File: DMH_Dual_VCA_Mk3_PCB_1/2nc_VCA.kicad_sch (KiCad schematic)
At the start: 38 parts, among them Q5 BC548, Q6 BC548, Q7 BC548, Q8 BC548, SW1 SW_DPDT_OnOffOn, SW2 SW_DPDT_3way, U3 TL074, U4 TL074

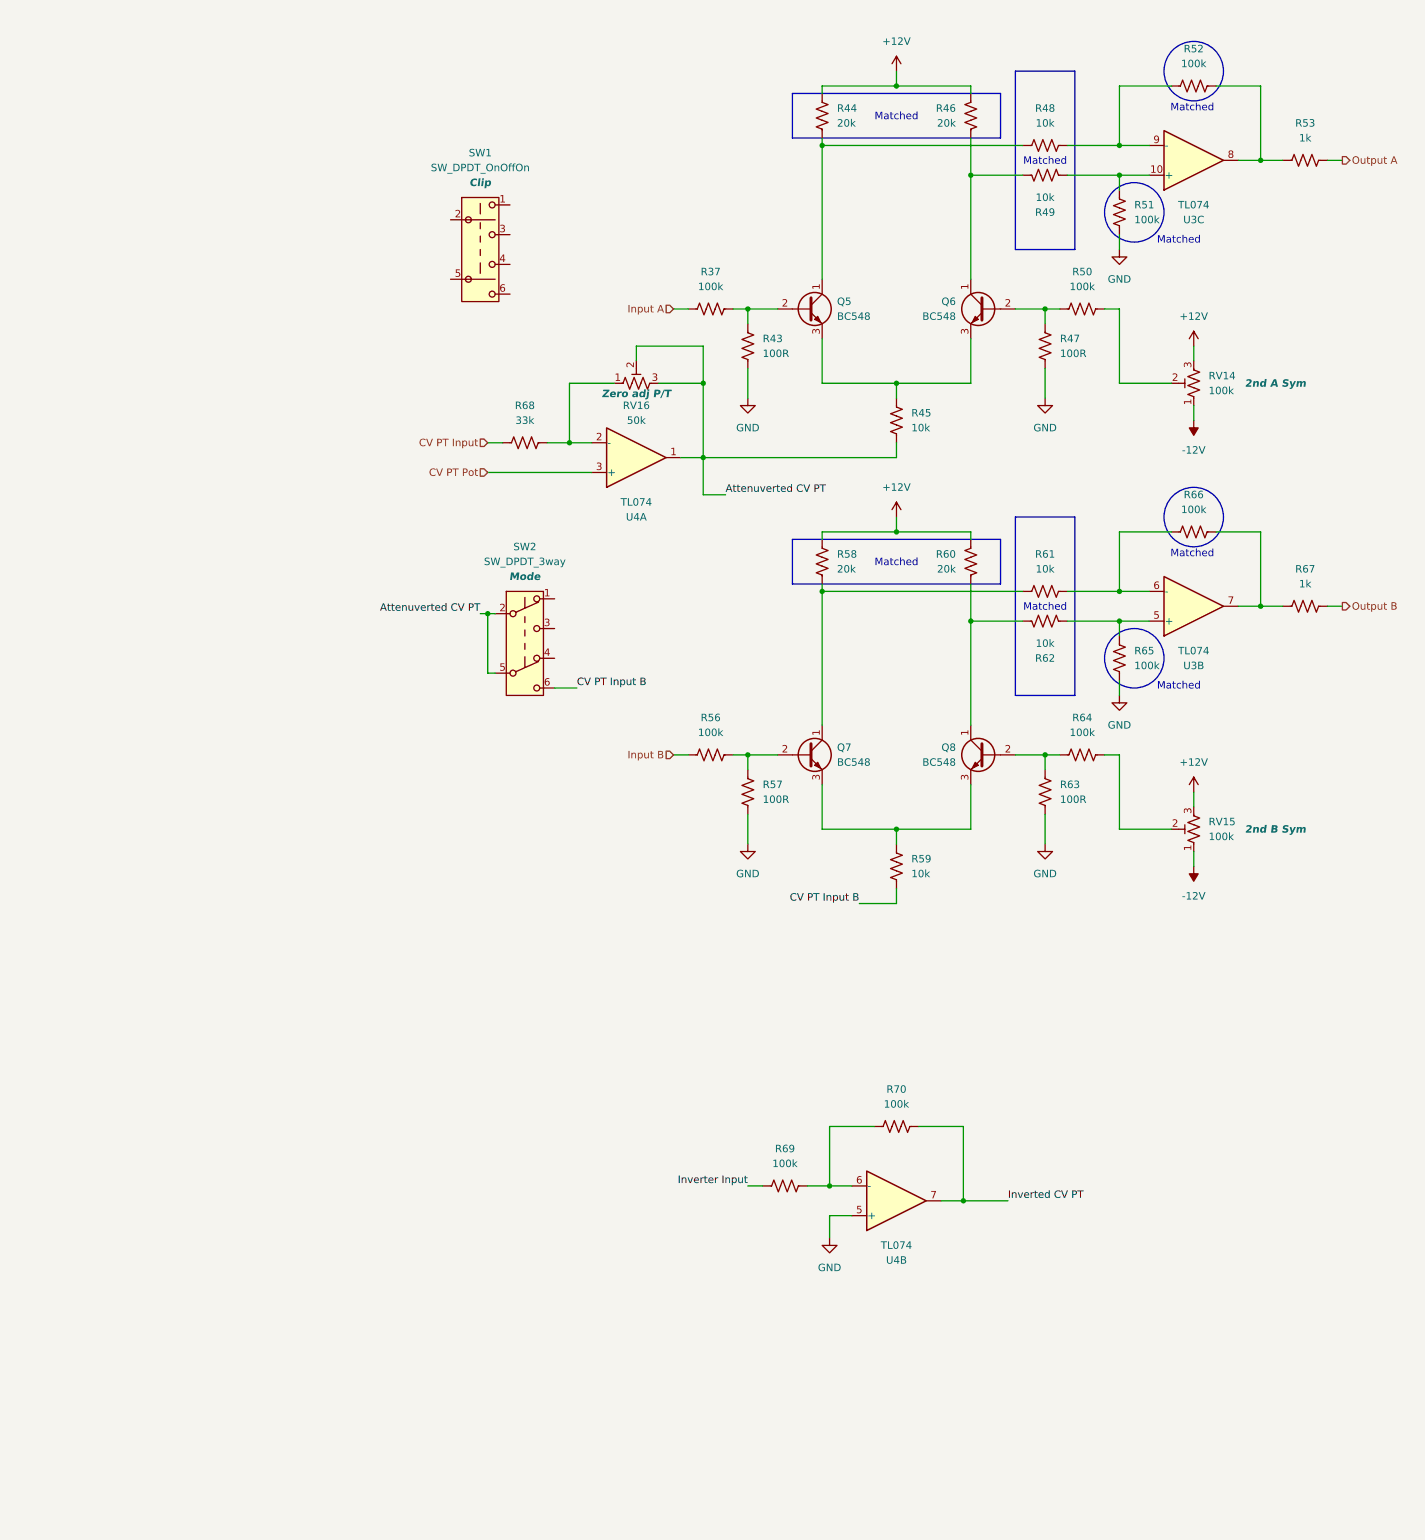
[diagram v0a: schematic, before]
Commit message: Mode switching design in progress
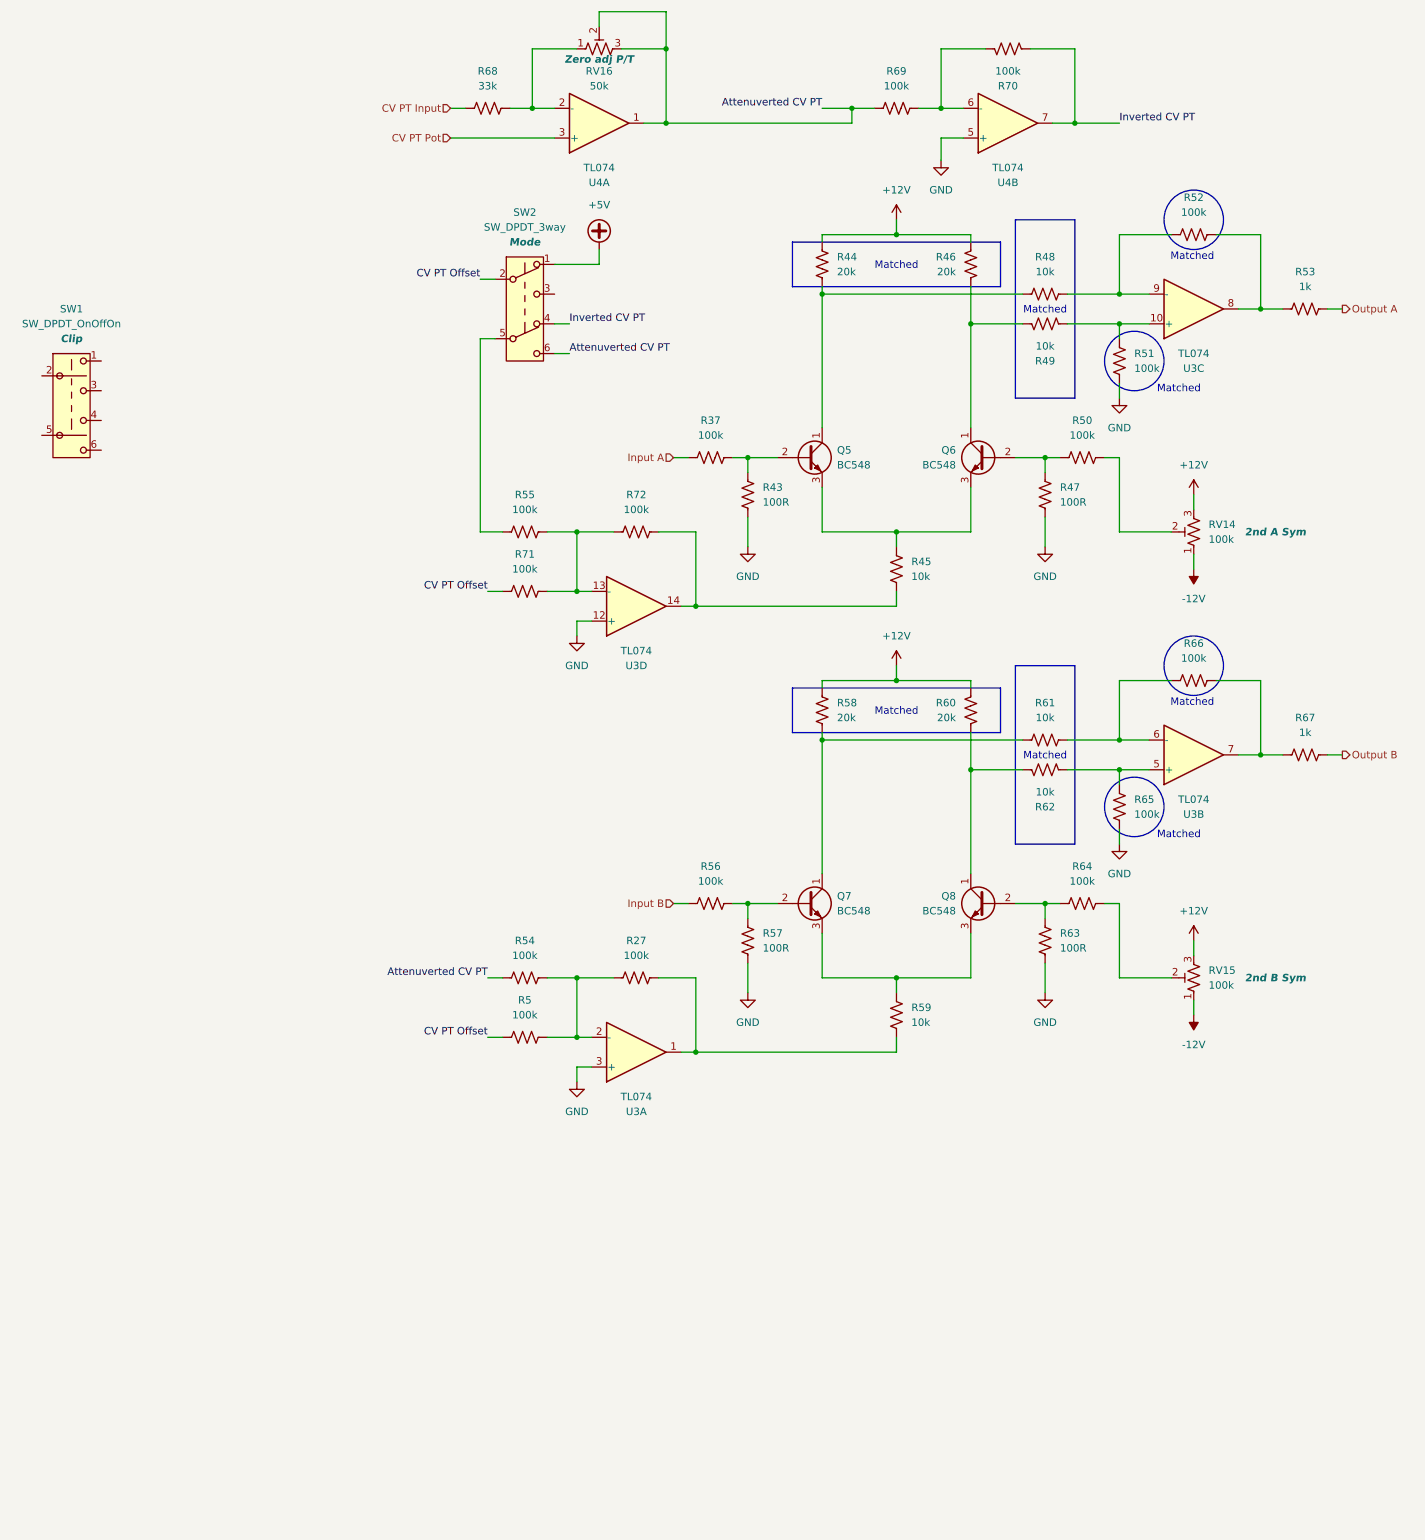
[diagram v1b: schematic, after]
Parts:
- added R27, R5, R54, R55, R71, R72: 100k, Resistor_THT:R_Axial_DIN0207_L6.3mm_D2.5mm_P7.62mm_Horizontal, symbol Device:R_US
- added unit 1 of U3
- added unit 4 of U3
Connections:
- net Inverter Input is gone; now on net Attenuverted CV PT: R69.1
- net Attenuverted CV PT: now also SW2.6 (C), R54.1; no longer R45.1, SW2.2 (B), SW2.5 (B)
- net GND: now also U3.12 (+), U3.3 (+)
- net Inverted CV PT: now also SW2.4 (A)
- net +5V: now reaches SW2.1 (A)
- net CV PT Input B: no longer names the net of R59.1
- net CV PT Input B: now also R27.2, U3.1; no longer SW2.6 (C)
- new net: R55.2, R71.2, R72.1, U3.13 (-)
- new net: R45.1, R72.2, U3.14
- new net: R27.1, R5.2, R54.2, U3.2 (-)
- new net: R55.1, SW2.5 (B)
- new net CV PT Offset: R5.1, R71.1, SW2.2 (B)
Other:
- moved on the sheet: Q5, Q6, Q7, Q8, R37, R43, R44, R45, R46, R47, R48, R49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

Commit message: 2nd VCA design done
Clipping design in progress
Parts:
- removed R53, R67: 1k, Resistor_THT:R_Axial_DIN0207_L6.3mm_D2.5mm_P7.62mm_Horizontal, symbol Device:R_US
- removed U4: TL074, Package_DIP:DIP-14_W7.62mm_Socket, symbol Amplifier_Operational:TL074
- added C11: 22pF, Capacitor_THT:C_Disc_D3.0mm_W2.0mm_P2.50mm, symbol Device:C
- added D3, D4: 1N4148, Diode_THT:D_DO-35_SOD27_P7.62mm_Horizontal, symbol Diode:1N4148
- added R74, R75, R76: 100k, Resistor_THT:R_Axial_DIN0207_L6.3mm_D2.5mm_P7.62mm_Horizontal, symbol Device:R_US
- added R77, R78: 20k, Resistor_THT:R_Axial_DIN0207_L6.3mm_D2.5mm_P7.62mm_Horizontal, symbol Device:R_US
- added R79: 10k, Resistor_THT:R_Axial_DIN0207_L6.3mm_D2.5mm_P7.62mm_Horizontal, symbol Device:R_US
- added U4: TL072, Package_DIP:DIP-8_W7.62mm_Socket, symbol Amplifier_Operational:TL072
- added U7: TL074, Package_DIP:DIP-14_W7.62mm_Socket, symbol Amplifier_Operational:TL074
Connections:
- net Attenuverted CV PT: now also U4.1
- net GND: now also R76.2, U4.5 (+), U7.10 (+), U7.12 (+)
- net Inverted CV PT: now also U4.7
- net Output A: now also R52.1, U3.8
- net Output B: now also R66.1, U3.7
- net at R68.2, RV16.1: now also U4.2 (-)
- net at R69.2, R70.1: now also U4.6 (-)
- net Balanced Offset: now reaches SW2.3 (C)
- net Balanced Offset: now also R78.1, U7.8
- new net: C11.1, D3.1 (K), D4.2 (A), U7.1
- new net: C11.2, D3.2 (A), R74.2, U7.2 (-)
- new net: D4.1 (K), R76.1, U7.5 (+)
- new net: R74.1, R75.2, U7.6 (-)
- new net: R75.1, R77.2, U7.7
- new net: R77.1, R78.2, R79.2, U7.9 (-)
- new net: U7.13 (-), U7.14
- new net -5V: R79.1
- new net CV PT Pot G1: U4.3 (+)
- new net CV PT Pot G2: U7.3 (+)
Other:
- moved on the sheet: R68, RV16, SW2

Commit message: Designed clip and dist circuit
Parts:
- removed SW1: SW_DPDT_OnOffOn, SynthStuff:Toggle_Switch_2_Poles_TE, symbol SynthStuff:Switch_DPDT_OnOffOn
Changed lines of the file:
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@@
+			)
+		)
+		(property "Sim.Device" "NPN"
+			(at 86.36 88.9 0)
+			(effects
+				(font
+					(size 1.27 1.27)
+				)
+				(hide yes)
+			)
+		)
+		(property "Sim.Pins" "1=C 2=B 3=E"
+			(at 86.36 88.9 0)
+			(effects
+				(font
+					(size 1.27 1.27)
+				)
+				(hide yes)
 			)
 		)
@@
 			)
 		)
+		(property "Sim.Device" "NPN"
+			(at 116.84 165.1 0)
+			(effects
+				(font
+					(size 1.27 1.27)
+				)
+				(hide yes)
+			)
+		)
+		(property "Sim.Pins" "1=C 2=B 3=E"
+			(at 116.84 165.1 0)
+			(effects
+				(font
+					(size 1.27 1.27)
+				)
+				(hide yes)
+			)
+		)
 		(pin "3"
 		)
@@
 			)
 		)
+		(property "Sim.Device" "NPN"
+			(at 116.84 88.9 0)
+			(effects
+				(font
+					(size 1.27 1.27)
+				)
+				(hide yes)
+			)
+		)
+		(property "Sim.Pins" "1=C 2=B 3=E"
+			(at 116.84 88.9 0)
+			(effects
+				(font
+					(size 1.27 1.27)
+				)
+				(hide yes)
+			)
+		)
 		(pin "3"
 		)
@@
 		)
 		(property "Description" "0.1A Ic, 30V Vce, Small Signal NPN Transistor, TO-92"
+			(at 86.36 165.1 0)
+			(effects
+				(font
+					(size 1.27 1.27)
+				)
+				(hide yes)
+			)
+		)
+		(property "Sim.Device" "NPN"
+			(at 86.36 165.1 0)
+			(effects
+				(font
+					(size 1.27 1.27)
+				)
+				(hide yes)
+			)
+		)
+		(property "Sim.Pins" "1=C 2=B 3=E"
 			(at 86.36 165.1 0)
 			(effects
@@
 					(unit 1)
 				)
-			)
-		)
-	)
-	(symbol
-		(lib_id "SynthStuff:Switch_DPDT_OnOffOn")
-		(at -39.37 80.01 0)
-		(unit 1)
-		(exclude_from_sim no)
-		(in_bom yes)
-		(on_board yes)
-		(dnp no)
-		(fields_autoplaced yes)
-		(property "Reference" "SW1"
-			(at -39.37 63.5 0)
-			(effects
-				(font
-					(size 1.27 1.27)
-				)
-			)
-		)
-		(property "Value" "SW_DPDT_OnOffOn"
-			(at -39.37 66.04 0)
-			(effects
-				(font
-					(size 1.27 1.27)
-				)
-			)
-		)
-		(property "Footprint" "SynthStuff:Toggle_Switch_2_Poles_TE"
-			(at -39.37 74.93 0)
-			(effects
-				(font
-					(size 1.27 1.27)
-				)
-				(hide yes)
-			)
-		)
-		(property "Datasheet" "~"
-			(at -39.37 74.93 0)
-			(effects
-				(font
-					(size 1.27 1.27)
-				)
-				(hide yes)
-			)
-		)
-		(property "Description" "DPDT switch, ON-OFF-ON"
-			(at -39.37 80.01 0)
-			(effects
-				(font
-					(size 1.27 1.27)
-				)
-				(hide yes)
-			)
-		)
-		(property "Function" "Clip"
-			(at -39.37 68.58 0)
-			(effects
-				(font
-					(size 1.27 1.27)
-					(thickness 0.254)
-					(bold yes)
-					(italic yes)
-				)
-			)
-		)
-		(pin "3"
-		)
-		(pin "1"
-		)
-		(pin "2"
-		)
-		(pin "4"
-		)
-		(pin "5"
-		)
-		(pin "6"
-		)
-		(instances
-			(project "DMH_Dual_VCA_Mk3_PCB_1"
-				(path "/58f4306d-5387-4983-bb08-41a2313fd315/8ee005da-7ca8-4d1e-92f5-43ab10d67fe9"
-					(reference "SW1")
-					(unit 1)
-				)
